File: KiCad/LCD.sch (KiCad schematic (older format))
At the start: 3 parts

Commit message: v1_final
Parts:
- renumbered LCD to LCD1, Potenciometro_10k to Potenciometro_10k1, R_D+ to R_D+1
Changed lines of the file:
@@
 $EndDescr
 $Comp
-L Display_Character:RC1602A LCD
+L Display_Character:RC1602A LCD1
 U 1 1 60AAFF17
 P 4900 3200
-F 0 "LCD" H 4900 4081 50  0000 C CNN
+F 0 "LCD1" H 4900 4081 50  0000 C CNN
 F 1 "RC1602A" H 4900 3990 50  0000 C CNN
 F 2 "Display:RC1602A" H 5000 2400 50  0001 C CNN
@@
 	4900 4000 4900 3900
 $Comp
-L Device:R_US R_D+
+L Device:R_US R_D+1
 U 1 1 60AB2FE4
 P 5500 3650
-F 0 "R_D+" H 5568 3696 50  0000 L CNN
+F 0 "R_D+1" H 5568 3696 50  0000 L CNN
 F 1 "560" H 5568 3605 50  0000 L CNN
 F 2 "" V 5540 3640 50  0001 C CNN
@@
 Vcc_5v
 $Comp
-L Device:R_POT_TRIM_US Potenciometro_10k
+L Device:R_POT_TRIM_US Potenciometro_10k1
 U 1 1 60AB7B9F
 P 5650 3000
-F 0 "Potenciometro_10k" H 5582 2954 50  0000 R CNN
+F 0 "Potenciometro_10k1" H 5582 2954 50  0000 R CNN
 F 1 "10k" H 5582 3045 50  0000 R CNN
 F 2 "" H 5650 3000 50  0001 C CNN

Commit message: adição departe dos footprints
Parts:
- LCD1: footprint Display:RC1602A -> Display:WC1602A
- Potenciometro_10k1: footprint (none) -> Potentiometer_THT:Potentiometer_Bourns_3296W_Vertical
- R_D+1: footprint (none) -> Resistor_SMD:R_0805_2012Metric
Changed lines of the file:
@@
 $Descr A4 11693 8268
 encoding utf-8
-Sheet 5 9
+Sheet 3 10
 Title ""
 Date ""
@@
 F 0 "LCD1" H 4900 4081 50  0000 C CNN
 F 1 "RC1602A" H 4900 3990 50  0000 C CNN
-F 2 "Display:RC1602A" H 5000 2400 50  0001 C CNN
+F 2 "Display:WC1602A" H 5000 2400 50  0001 C CNN
 F 3 "http://www.raystar-optronics.com/down.php?ProID=18" H 5000 3100 50  0001 C CNN
 	1    4900 3200
@@
 F 0 "R_D+1" H 5568 3696 50  0000 L CNN
 F 1 "560" H 5568 3605 50  0000 L CNN
-F 2 "" V 5540 3640 50  0001 C CNN
+F 2 "Resistor_SMD:R_0805_2012Metric" V 5540 3640 50  0001 C CNN
 F 3 "~" H 5500 3650 50  0001 C CNN
 	1    5500 3650
@@
 F 0 "Potenciometro_10k1" H 5582 2954 50  0000 R CNN
 F 1 "10k" H 5582 3045 50  0000 R CNN
-F 2 "" H 5650 3000 50  0001 C CNN
+F 2 "Potentiometer_THT:Potentiometer_Bourns_3296W_Vertical" H 5650 3000 50  0001 C CNN
 F 3 "~" H 5650 3000 50  0001 C CNN
 	1    5650 3000

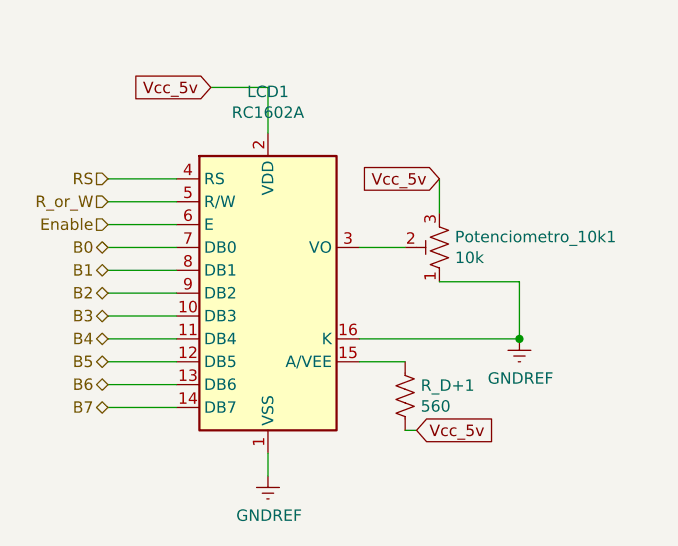
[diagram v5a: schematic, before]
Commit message: correção P1: LCD e Capacitores
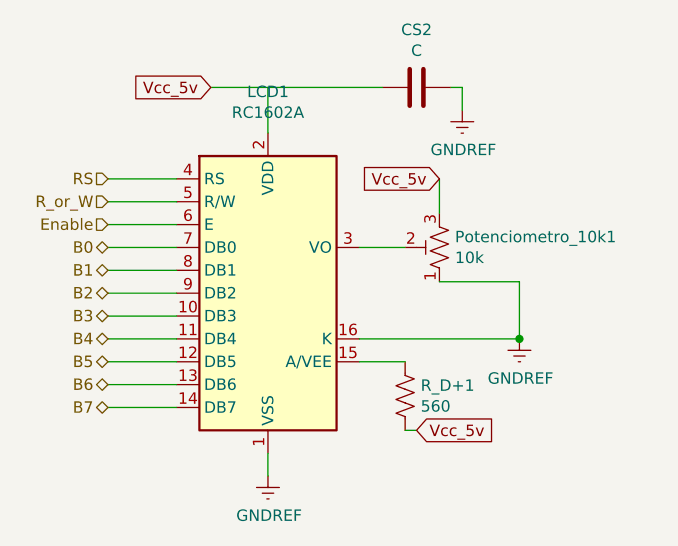
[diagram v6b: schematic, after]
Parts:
- added CS2: C, Capacitor_SMD:C_0805_2012Metric_Pad1.18x1.45mm_HandSolder, symbol Device:C
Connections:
- net GNDREF: now also CS2.1
- net Vcc_5v: now also CS2.2
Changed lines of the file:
@@
 Wire Wire Line
 	4200 3000 4500 3000
+$Comp
+L power:GNDREF #PWR?
+U 1 1 60FAD465
+P 5750 2400
+AR Path="/60FAD465" Ref="#PWR?"  Part="1"
+AR Path="/60AF7D01/60FAD465" Ref="#PWR03"  Part="1"
+F 0 "#PWR03" H 5750 2150 50  0001 C CNN
+F 1 "GNDREF" H 5755 2227 50  0000 C CNN
+F 2 "" H 5750 2400 50  0001 C CNN
+F 3 "" H 5750 2400 50  0001 C CNN
+	1    5750 2400
+	1    0    0    -1
+$EndComp
+$Comp
+L Device:C CS?
+U 1 1 60FAD46B
+P 5550 2300
+AR Path="/60FAD46B" Ref="CS?"  Part="1"
+AR Path="/60AF7D01/60FAD46B" Ref="CS2"  Part="1"
+F 0 "CS2" V 5298 2300 50  0000 C CNN
+F 1 "C" V 5389 2300 50  0000 C CNN
+F 2 "Capacitor_SMD:C_0805_2012Metric_Pad1.18x1.45mm_HandSolder" H 5588 2150 50  0001 C CNN
+F 3 "~" H 5550 2300 50  0001 C CNN
+	1    5550 2300
+	0    1    1    0
+$EndComp
+Wire Wire Line
+	5750 2400 5750 2300
+Wire Wire Line
+	5750 2300 5700 2300
+Wire Wire Line
+	5400 2300 4900 2300
 $EndSCHEMATC

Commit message: Valores dos capacitores CS
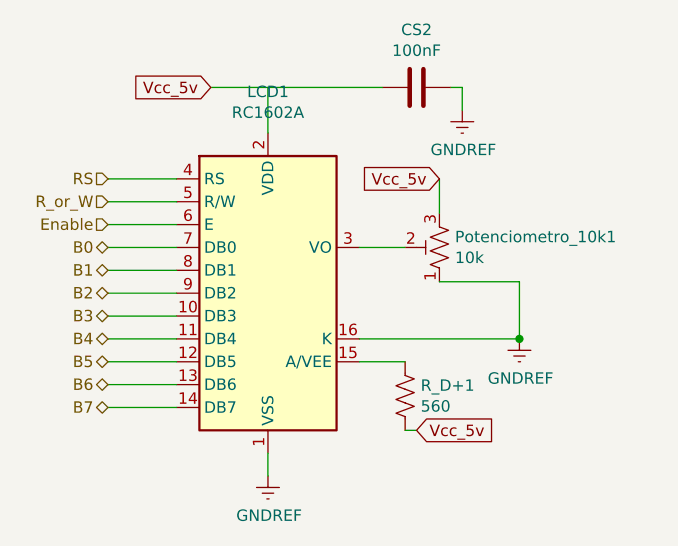
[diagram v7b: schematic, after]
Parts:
- CS2: value C -> 100nF
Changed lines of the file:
@@
 AR Path="/60AF7D01/60FAD46B" Ref="CS2"  Part="1"
 F 0 "CS2" V 5298 2300 50  0000 C CNN
-F 1 "C" V 5389 2300 50  0000 C CNN
+F 1 "100nF" V 5389 2300 50  0000 C CNN
 F 2 "Capacitor_SMD:C_0805_2012Metric_Pad1.18x1.45mm_HandSolder" H 5588 2150 50  0001 C CNN
 F 3 "~" H 5550 2300 50  0001 C CNN
